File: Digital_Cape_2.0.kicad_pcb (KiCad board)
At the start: 2 copper layers, 57.2 x 63.5 mm, 15 parts, among them J1 RJ45, J2 RJ45, P8 BeagleBone_Black_Header, P9 BeagleBone_Black_Header

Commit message: Update of KiCad files
My apologies I'm still learning! Files from 02-13-2021 Hangar session
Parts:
- added H1: MountingHole, MountingHole:MountingHole_3.2mm_M3, F.Cu at (88.3, 121.3)
- added H2: MountingHole, MountingHole:MountingHole_3.2mm_M3, F.Cu at (136.5, 121.3)
- added H3: MountingHole, MountingHole:MountingHole_3.2mm_M3, F.Cu at (133.3, 55.2)
- added H4: MountingHole, MountingHole:MountingHole_3.2mm_M3, F.Cu at (91.4, 55.2)
- added R1: 4.7k, Resistor_THT:R_Axial_DIN0204_L3.6mm_D1.6mm_P5.08mm_Horizontal, F.Cu at (110.2, 108.7)
- added R2: 4.7k, Resistor_THT:R_Axial_DIN0204_L3.6mm_D1.6mm_P5.08mm_Horizontal, F.Cu at (119.4, 80.8)
- C1, C2, C3, C4, C5, CP1, CP2: footprint Capacitor_SMD:CP_Elec_4x4.5 -> Capacitor_THT:C_Disc_D3.0mm_W2.0mm_P2.50mm
- moved J1 56.5 mm to (116.8, 121.3)
- moved J2 56.5 mm to (97.8, 121.3)
- moved C4 28.9 mm to (98.0, 91.4), turned to 180 degrees
- moved RP2 23.8 mm to (99.1, 110.7)
- moved C2 23.7 mm to (121.4, 107.2)
- moved RP1 23.0 mm to (95.5, 107.7), turned to 270 degrees
- moved C3 21.6 mm to (112.8, 98.0), turned to 180 degrees
- moved LSM9_DS1_REF1 16.0 mm to (118.9, 100.6), turned to 90 degrees
- moved CP2 15.0 mm to (97.5, 103.1)
- moved C5 14.2 mm to (110.2, 93.5), turned to 0 degrees
- moved BME_280_REF1 13.1 mm to (103.6, 106.7), turned to 270 degrees
- moved CP1 9.45 mm to (102.6, 99.6)
- moved C1 8.19 mm to (113.3, 102.1), turned to 180 degrees
- moved P8 2.30 mm to (88.9, 60.3)
- moved P9 1.91 mm to (133.3, 60.3)
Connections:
- BME_280_REF1 pad 5: Net-(BME_280_REF1-Pad5) -> GND
- J1 pad 4: /GND1 -> GND
- J1 pad 5: /GND2 -> GND
- J2 pad 4: /GND1 -> GND
- J2 pad 5: /GND2 -> GND
- LSM9_DS1_REF1 pad 5: Net-(LSM9_DS1_REF1-Pad5) -> GND
- P8 pad 1: GNDD -> GND
- P8 pad 2: GNDD -> GND
- P9 pad 1: GNDD -> GND
- P9 pad 2: GNDD -> GND
- P9 pad 34: GNDA_ADC -> GND
- P9 pad 43: GNDD -> GND
- P9 pad 44: GNDD -> GND
- P9 pad 45: GNDD -> GND
- P9 pad 46: GNDD -> GND
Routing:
- net /I2C2_SDA: track 0.78 -> 112.5 mm, vias 0 -> 2
- net /I2C1_SCL: track 0.00 -> 95.5 mm, vias 0 -> 1
- net /I2C1_SDA: track 0.00 -> 95.2 mm, vias 0 -> 3
- net /Vdd_IO: track 0.72 -> 95.4 mm, vias 0 -> 2
- net +5V: track 0.00 -> 87.7 mm, vias 0 -> 1
- net /I2C2_SCL: track 0.00 -> 74.6 mm, vias 0 -> 2
- net /Vdd: track 0.00 -> 34.7 mm, vias 0 -> 2
- net Net-(C5-Pad2): track 0.00 -> 10.2 mm
- net GND: track 0.00 -> 7.73 mm
- net Net-(C1-Pad1): track 0.00 -> 4.55 mm
- net GNDD: track 2.52 -> 0.00 mm
- net /uart2_rxd: track 0.00 -> 0.78 mm
- added copper zone on B.Cu, net GND
- added copper zone on F.Cu, net GND
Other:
- board size 57.2 x 63.5 mm -> 54.6 x 86.4 mm
- net class Default: clearance 0.2 -> 0.127
- rule trace_clearance: 0.2 -> 0.127

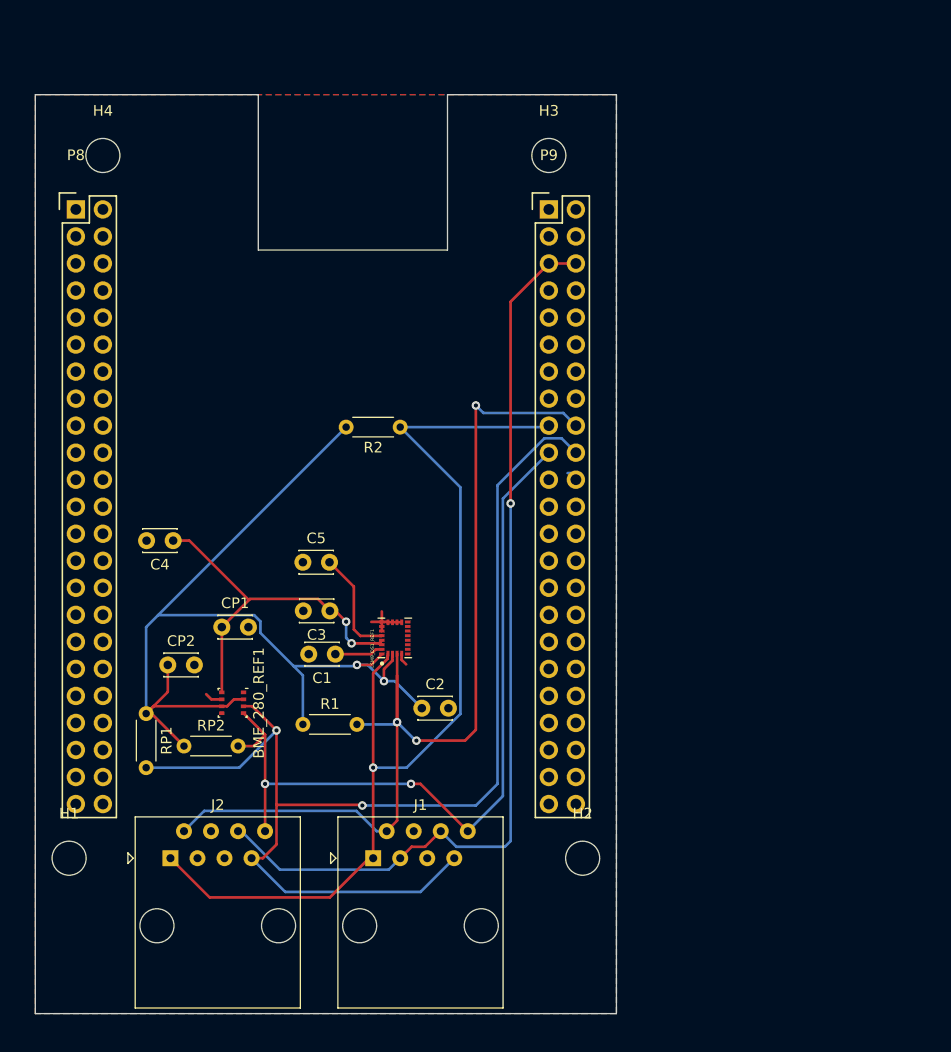
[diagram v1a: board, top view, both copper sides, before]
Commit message: Update board to fit BBB cape spec
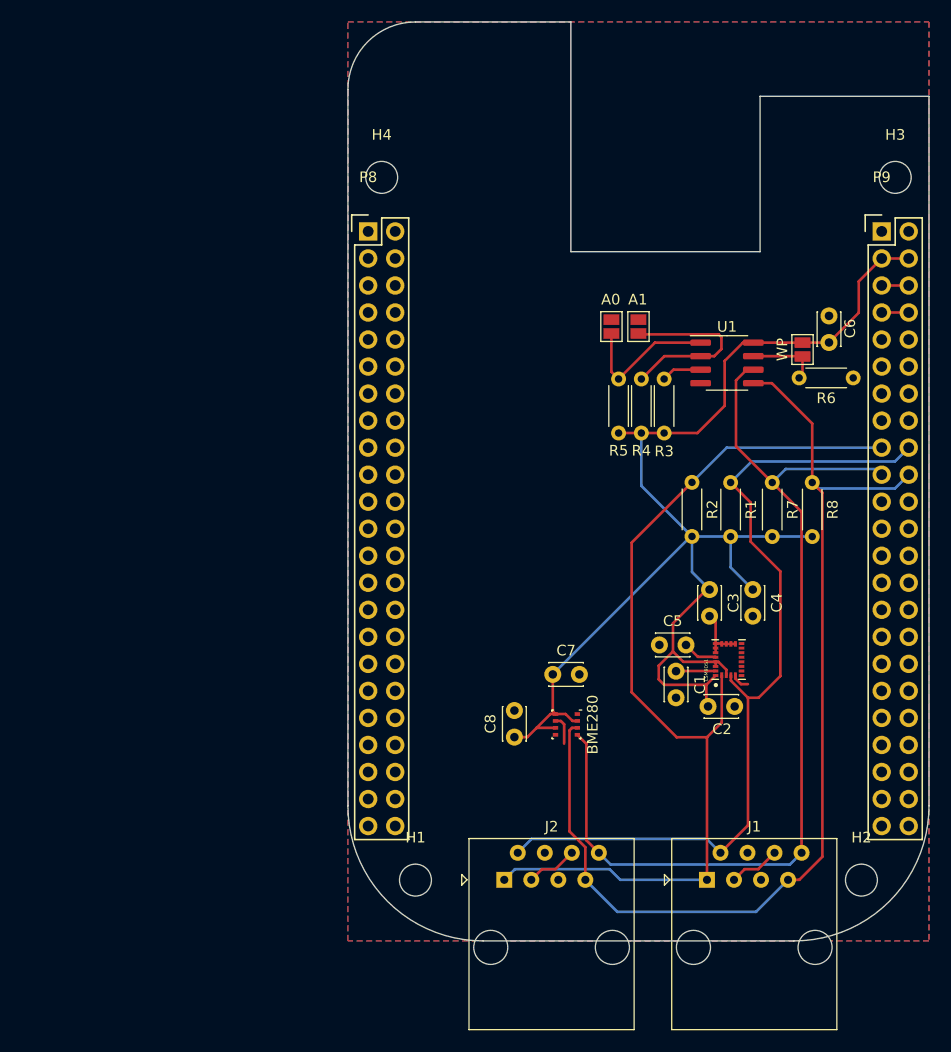
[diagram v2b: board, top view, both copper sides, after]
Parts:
- removed BME_280_REF1: BME_280, Package_LGA:Bosch_LGA-8_2.5x2.5mm_P0.65mm_ClockwisePinNumbering
- removed CP1, CP2: 100nF, Capacitor_THT:C_Disc_D3.0mm_W2.0mm_P2.50mm
- removed LSM9_DS1_REF1: LSM9_DS1, LSM9_DS1:LSM9_DS1
- removed RP1, RP2: 4.7k, Resistor_THT:R_Axial_DIN0204_L3.6mm_D1.6mm_P5.08mm_Horizontal
- added BME280: BME_280, Package_LGA:Bosch_LGA-8_2.5x2.5mm_P0.65mm_ClockwisePinNumbering, F.Cu at (135.0, 108.7)
- added C6: 0.1u, Capacitor_THT:C_Disc_D3.0mm_W2.0mm_P2.50mm, F.Cu at (159.7, 72.8)
- added C7: 100nF, Capacitor_THT:C_Disc_D3.0mm_W2.0mm_P2.50mm, F.Cu at (133.7, 104.0)
- added C8: 100nF, Capacitor_THT:C_Disc_D3.0mm_W2.0mm_P2.50mm, F.Cu at (130.1, 109.9)
- added JP1: A0, Jumper:SolderJumper-2_P1.3mm_Open_Pad1.0x1.5mm, F.Cu at (139.2, 71.3)
- added JP2: A1, Jumper:SolderJumper-2_P1.3mm_Open_Pad1.0x1.5mm, F.Cu at (141.8, 71.3)
- added JP3: WP, Jumper:SolderJumper-2_P1.3mm_Open_Pad1.0x1.5mm, F.Cu at (157.2, 73.5)
- added LSM9DS1: LSM9_DS1, LSM9_DS1:LSM9_DS1, F.Cu at (150.2, 102.6)
- added R3: 4.7k, Resistor_THT:R_Axial_DIN0204_L3.6mm_D1.6mm_P5.08mm_Horizontal, F.Cu at (144.2, 81.3)
- added R4: 4.7k, Resistor_THT:R_Axial_DIN0204_L3.6mm_D1.6mm_P5.08mm_Horizontal, F.Cu at (142.0, 81.3)
- added R5: 4.7k, Resistor_THT:R_Axial_DIN0204_L3.6mm_D1.6mm_P5.08mm_Horizontal, F.Cu at (139.9, 81.3)
- added R6: 10k, Resistor_THT:R_Axial_DIN0204_L3.6mm_D1.6mm_P5.08mm_Horizontal, F.Cu at (156.9, 76.1)
- added R7: 4.7k, Resistor_THT:R_Axial_DIN0204_L3.6mm_D1.6mm_P5.08mm_Horizontal, F.Cu at (154.3, 86.0)
- added R8: 4.7k, Resistor_THT:R_Axial_DIN0204_L3.6mm_D1.6mm_P5.08mm_Horizontal, F.Cu at (158.1, 86.0)
- added U1: CAT24C256, Package_SO:SOIC-8_3.9x4.9mm_P1.27mm, F.Cu at (150.1, 74.7)
- H1, H2, H3, H4: footprint MountingHole:MountingHole_3.2mm_M3 -> MountingHole:MountingHole_3mm
- moved C4 54.7 mm to (152.5, 96.0), turned to 270 degrees
- moved R1 46.2 mm to (150.4, 86.0), turned to 270 degrees
- moved C3 35.7 mm to (148.5, 96.0), turned to 270 degrees
- moved C5 34.4 mm to (143.7, 101.2)
- moved H3 32.6 mm to (165.9, 57.3)
- moved H1 32.6 mm to (120.8, 123.3)
- moved C1 32.1 mm to (145.3, 103.7), turned to 270 degrees
- moved J1 31.4 mm to (148.2, 123.3)
- moved J2 31.4 mm to (129.2, 123.3)
- moved P9 31.3 mm to (164.6, 62.4)
- moved R2 27.9 mm to (146.8, 86.0), turned to 270 degrees
- moved P8 27.5 mm to (116.4, 62.4)
- moved C2 26.9 mm to (148.3, 107.0)
- moved H4 26.3 mm to (117.6, 57.3)
- moved H2 26.3 mm to (162.7, 123.3)
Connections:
- C2 pad 1: /Vdd_IO -> +3V3
- C3 pad 1: /Vdd -> +3V3
- C4 pad 1: /Vdd -> +3V3
- P8 pad 10: Net-(P8-Pad10) -> (no net)
- P8 pad 11: Net-(P8-Pad11) -> (no net)
- P8 pad 12: Net-(P8-Pad12) -> (no net)
- P8 pad 13: Net-(P8-Pad13) -> (no net)
- P8 pad 14: Net-(P8-Pad14) -> (no net)
- P8 pad 15: Net-(P8-Pad15) -> (no net)
- P8 pad 16: Net-(P8-Pad16) -> (no net)
- P8 pad 17: Net-(P8-Pad17) -> (no net)
- P8 pad 18: Net-(P8-Pad18) -> (no net)
- P8 pad 19: Net-(P8-Pad19) -> (no net)
- P8 pad 20: Net-(P8-Pad20) -> (no net)
- P8 pad 21: Net-(P8-Pad21) -> (no net)
- P8 pad 22: Net-(P8-Pad22) -> (no net)
- P8 pad 23: Net-(P8-Pad23) -> (no net)
- P8 pad 24: Net-(P8-Pad24) -> (no net)
- P8 pad 25: Net-(P8-Pad25) -> (no net)
- P8 pad 26: Net-(P8-Pad26) -> (no net)
- P8 pad 27: Net-(P8-Pad27) -> (no net)
- P8 pad 28: Net-(P8-Pad28) -> (no net)
- P8 pad 29: Net-(P8-Pad29) -> (no net)
- P8 pad 3: Net-(P8-Pad3) -> (no net)
- P8 pad 30: Net-(P8-Pad30) -> (no net)
- P8 pad 31: Net-(P8-Pad31) -> (no net)
- P8 pad 32: Net-(P8-Pad32) -> (no net)
- P8 pad 33: Net-(P8-Pad33) -> (no net)
- P8 pad 34: Net-(P8-Pad34) -> (no net)
- P8 pad 35: Net-(P8-Pad35) -> (no net)
- P8 pad 36: Net-(P8-Pad36) -> (no net)
- P8 pad 37: Net-(P8-Pad37) -> (no net)
- P8 pad 38: Net-(P8-Pad38) -> (no net)
- P8 pad 39: Net-(P8-Pad39) -> (no net)
- P8 pad 4: Net-(P8-Pad4) -> (no net)
- P8 pad 40: Net-(P8-Pad40) -> (no net)
- P8 pad 41: Net-(P8-Pad41) -> (no net)
- P8 pad 42: Net-(P8-Pad42) -> (no net)
- P8 pad 43: Net-(P8-Pad43) -> (no net)
- P8 pad 44: Net-(P8-Pad44) -> (no net)
- P8 pad 45: Net-(P8-Pad45) -> (no net)
- P8 pad 46: Net-(P8-Pad46) -> (no net)
- P8 pad 5: Net-(P8-Pad5) -> (no net)
- P8 pad 6: Net-(P8-Pad6) -> (no net)
- P8 pad 7: Net-(P8-Pad7) -> (no net)
- P8 pad 8: Net-(P8-Pad8) -> (no net)
- P8 pad 9: Net-(P8-Pad9) -> (no net)
- P9 pad 10: SYS_RESETN -> (no net)
- P9 pad 11: Net-(P9-Pad11) -> (no net)
- P9 pad 12: Net-(P9-Pad12) -> (no net)
- P9 pad 13: Net-(P9-Pad13) -> (no net)
- P9 pad 14: Net-(P9-Pad14) -> (no net)
- P9 pad 15: Net-(P9-Pad15) -> (no net)
- P9 pad 16: Net-(P9-Pad16) -> (no net)
- P9 pad 21: /uart2_txd -> (no net)
- P9 pad 22: /uart2_rxd -> (no net)
- P9 pad 23: Net-(P9-Pad23) -> (no net)
- P9 pad 24: Net-(P9-Pad24) -> (no net)
- P9 pad 25: Net-(P9-Pad25) -> (no net)
- P9 pad 26: Net-(P9-Pad26) -> (no net)
- P9 pad 27: Net-(P9-Pad27) -> (no net)
- P9 pad 28: /spi1_cs0 -> (no net)
- P9 pad 29: /spi1_d0 -> (no net)
- P9 pad 30: /spi1_d1 -> (no net)
- P9 pad 31: /spi1_sclk -> (no net)
- P9 pad 32: VDD_ADC -> (no net)
- P9 pad 33: Net-(P9-Pad33) -> (no net)
- P9 pad 34: GND -> (no net)
- P9 pad 35: Net-(P9-Pad35) -> (no net)
- P9 pad 36: Net-(P9-Pad36) -> (no net)
- P9 pad 37: Net-(P9-Pad37) -> (no net)
- P9 pad 38: Net-(P9-Pad38) -> (no net)
- P9 pad 39: Net-(P9-Pad39) -> (no net)
- P9 pad 40: Net-(P9-Pad40) -> (no net)
- P9 pad 41: Net-(P9-Pad41) -> (no net)
- P9 pad 42: Net-(P9-Pad42) -> (no net)
- P9 pad 9: PWR_BUT -> (no net)
- R1 pad 1: /Vdd_IO -> /I2C1_SDA
- R1 pad 2: /I2C1_SDA -> +3V3
- R2 pad 2: /Vdd_IO -> +3V3
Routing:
- net +3V3: track 0.00 -> 129.2 mm
- net /Vdd_IO: track 95.4 -> 0.00 mm, vias 2 -> 0
- net +5V: track 87.7 -> 12.3 mm, vias 1 -> 0
- net /Vdd: track 34.7 -> 0.00 mm, vias 2 -> 0
- net Net-(JP2-Pad1): track 0.00 -> 17.7 mm
- net /I2C2_SCL: track 74.6 -> 91.9 mm, vias 2 -> 0
- net /I2C1_SDA: track 95.2 -> 80.7 mm, vias 3 -> 0
- net Net-(JP1-Pad1): track 0.00 -> 13.4 mm
- net /I2C2_SDA: track 112.5 -> 99.2 mm, vias 2 -> 0
- net Net-(C5-Pad2): track 10.2 -> 3.26 mm
- net Net-(JP3-Pad2): track 0.00 -> 6.78 mm
- net /I2C1_SCL: track 95.5 -> 89.8 mm, vias 1 -> 0
- net Net-(R3-Pad2): track 0.00 -> 3.79 mm
- net SYS_5V: track 0.00 -> 2.54 mm
- net GND: track 7.73 -> 10.0 mm
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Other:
- outline, holes or cut-outs redrawn

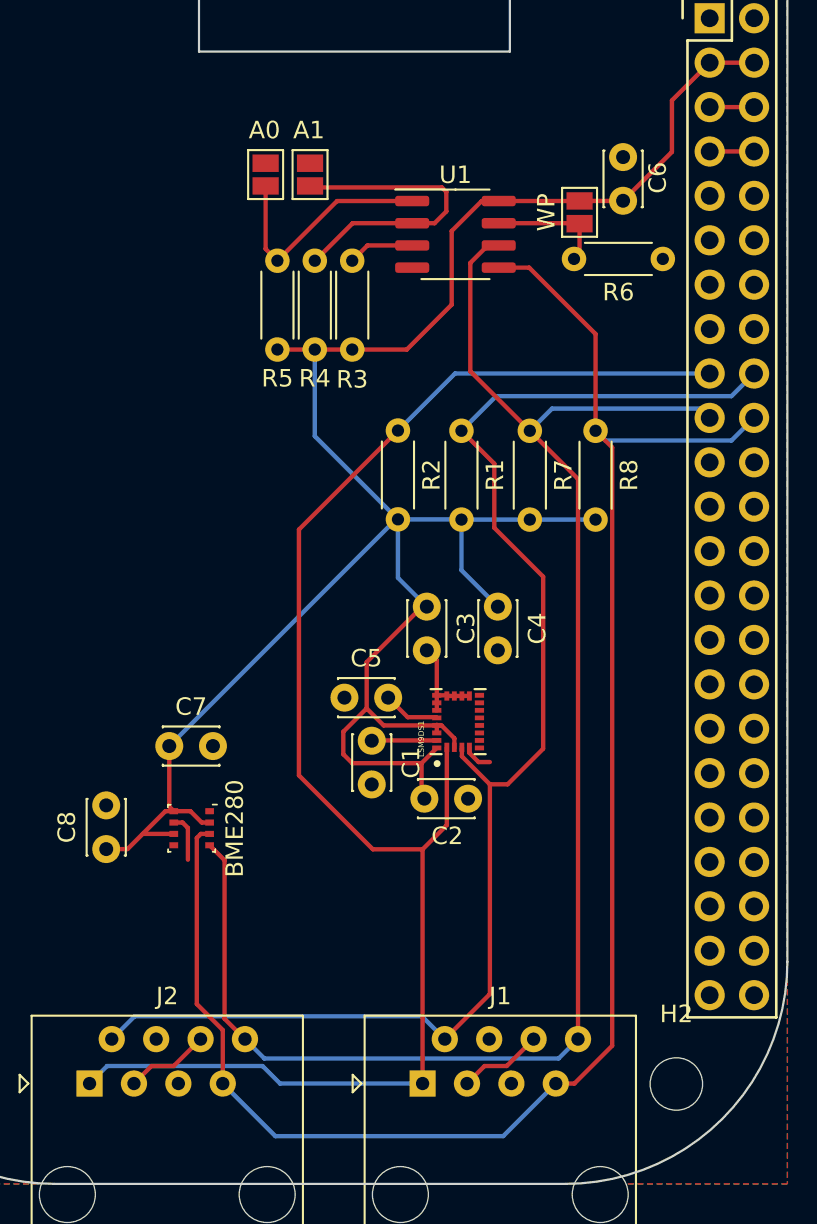
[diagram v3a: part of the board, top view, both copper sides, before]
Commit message: Fix LSM9DS1
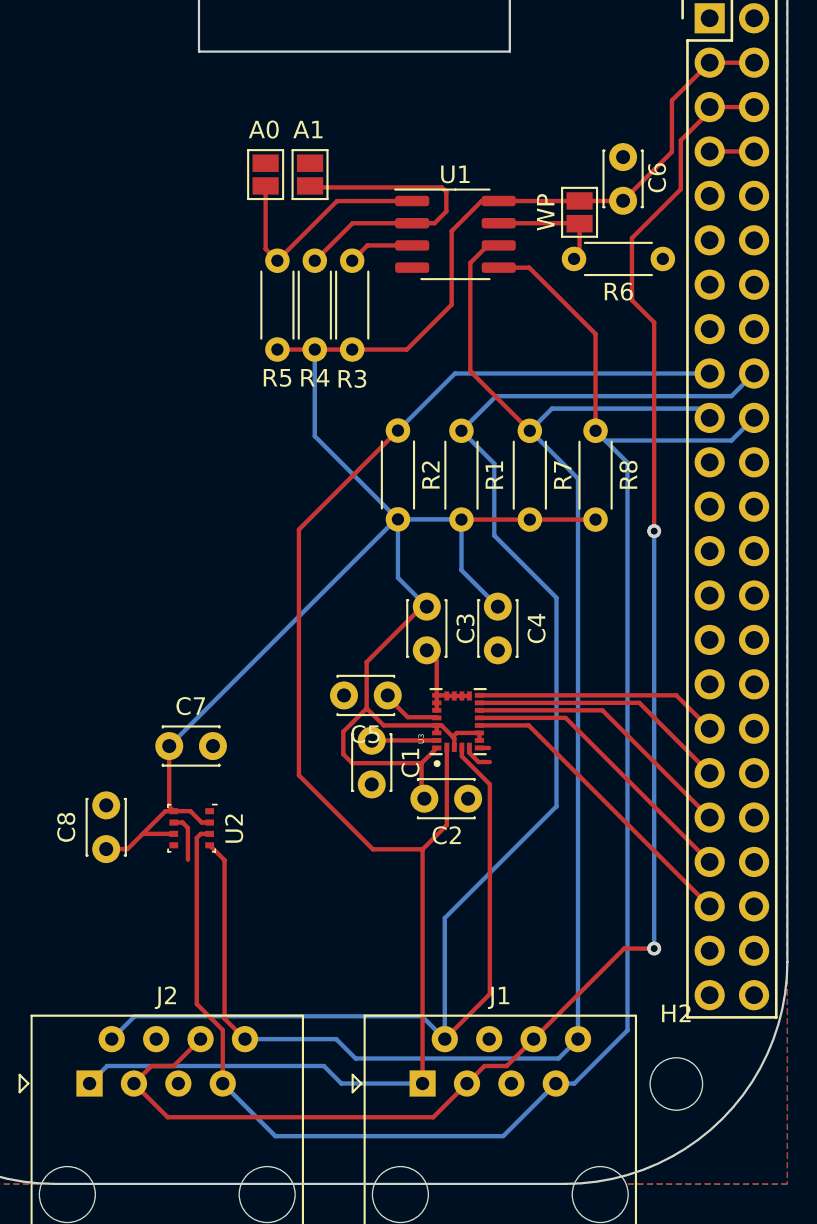
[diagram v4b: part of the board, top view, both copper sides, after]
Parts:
- moved C5 2.48 mm to (146.2, 101.1), turned to 180 degrees
- renumbered BME280 to U2, LSM9DS1 to U3
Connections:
- C5 pad 1: GND -> Net-(C5-Pad1)
- C5 pad 2: Net-(C5-Pad2) -> GND
- P9 pad 33: (no net) -> /LSM9_EN
- P9 pad 35: (no net) -> /INT2_A
- P9 pad 37: (no net) -> /INT1_A
- P9 pad 39: (no net) -> /DRDY_M
- P9 pad 41: (no net) -> /INT_M
- U3 pad 10: (no net) -> /DRDY_M
- U3 pad 11: (no net) -> /INT1_A
- U3 pad 12: (no net) -> /INT2_A
- U3 pad 13: (no net) -> /LSM9_EN
- U3 pad 21: Net-(C5-Pad2) -> Net-(C5-Pad1)
- U3 pad 6: (no net) -> GND
- U3 pad 7: (no net) -> +3V3
- U3 pad 8: (no net) -> +3V3
- U3 pad 9: (no net) -> /INT_M
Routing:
- net +5V: track 12.3 -> 92.5 mm, vias 0 -> 2
- net /INT_M: track 0.00 -> 17.5 mm
- net /DRDY_M: track 0.00 -> 16.6 mm
- net /INT1_A: track 0.00 -> 15.7 mm
- net /I2C1_SDA: track 80.7 -> 96.3 mm
- net /INT2_A: track 0.00 -> 14.8 mm
- net /LSM9_EN: track 0.00 -> 14.0 mm
- net Net-(C5-Pad2): track 3.26 -> 0.00 mm
- net Net-(C5-Pad1): track 0.00 -> 3.26 mm
- net +3V3: track 129.2 -> 131.3 mm
- net /I2C2_SDA: track 99.2 -> 99.9 mm
- net GND: track 10.0 -> 10.6 mm

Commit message: Switch pin headers to default libs
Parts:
- P8, P9: footprint Socket_BeagleBone_Black:Socket_BeagleBone_Black -> Connector_PinHeader_2.54mm:PinHeader_2x23_P2.54mm_Vertical
